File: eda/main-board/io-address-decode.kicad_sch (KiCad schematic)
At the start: 2 parts, among them U5 74HCT138

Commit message: Work on main board eda, interim
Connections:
- net IoSelect0: now also U5.15 (O0)
- net IoSelect1: now also U5.14 (O1)
- net IoSelect2: now also U5.13 (O2)
- net IoSelect3: now also U5.12 (O3)
- net IoSelect4: now also U5.11 (O4)
- net IoSelect5: now also U5.10 (O5)
- net IoSelect6: now also U5.9 (O6)
- net IoSelect7: now also U5.7 (O7)
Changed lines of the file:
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@@
     (stroke (width 0) (type default))
   )
-  (label "A8" (at 44.45 45.72 0)
+  (label "A8" (at 44.45 45.72 0) (fields_autoplaced)
     (effects (font (size 1.27 1.27)) (justify left bottom))
   )
-  (label "IoSelect5" (at 69.85 53.34 0)
+  (label "IoSelect5" (at 72.39 53.34 0) (fields_autoplaced)
     (effects (font (size 1.27 1.27)) (justify left bottom))
   )
-  (label "A6" (at 44.45 40.64 0)
+  (label "A6" (at 44.45 40.64 0) (fields_autoplaced)
     (effects (font (size 1.27 1.27)) (justify left bottom))
   )
-  (label "IoSelect1" (at 69.85 43.18 0)
+  (label "IoSelect1" (at 72.39 43.18 0) (fields_autoplaced)
     (effects (font (size 1.27 1.27)) (justify left bottom))
   )
-  (label "IoSelect0" (at 69.85 40.64 0)
+  (label "IoSelect0" (at 72.39 40.64 0) (fields_autoplaced)
     (effects (font (size 1.27 1.27)) (justify left bottom))
   )
-  (label "IoSelect2" (at 69.85 45.72 0)
+  (label "IoSelect2" (at 72.39 45.72 0) (fields_autoplaced)
     (effects (font (size 1.27 1.27)) (justify left bottom))
   )
-  (label "IoSelect4" (at 69.85 50.8 0)
+  (label "IoSelect4" (at 72.39 50.8 0) (fields_autoplaced)
     (effects (font (size 1.27 1.27)) (justify left bottom))
   )
-  (label "IoSelect7" (at 69.85 58.42 0)
+  (label "IoSelect7" (at 72.39 58.42 0) (fields_autoplaced)
     (effects (font (size 1.27 1.27)) (justify left bottom))
   )
-  (label "IoSelect6" (at 69.85 55.88 0)
+  (label "IoSelect6" (at 72.39 55.88 0) (fields_autoplaced)
     (effects (font (size 1.27 1.27)) (justify left bottom))
   )
-  (label "A7" (at 44.45 43.18 0)
+  (label "A7" (at 44.45 43.18 0) (fields_autoplaced)
     (effects (font (size 1.27 1.27)) (justify left bottom))
   )
-  (label "IoSelect3" (at 69.85 48.26 0)
+  (label "IoSelect3" (at 72.39 48.26 0) (fields_autoplaced)
     (effects (font (size 1.27 1.27)) (justify left bottom))
   )

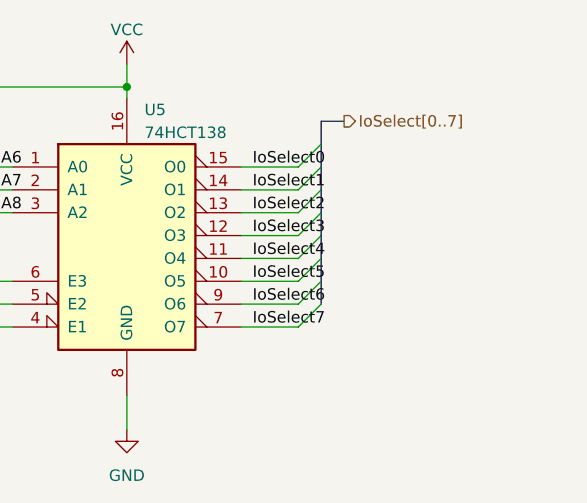
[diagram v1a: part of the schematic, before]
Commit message: EDA work for new expansion header
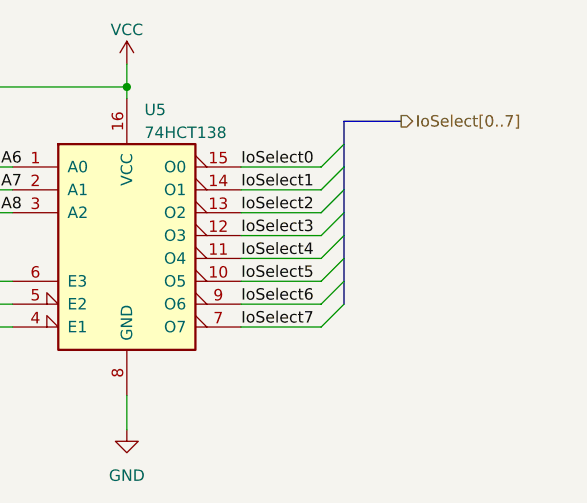
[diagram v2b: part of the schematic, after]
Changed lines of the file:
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@@
   (junction (at 41.91 58.42) (diameter 0) (color 0 0 0 0)
   )
-  (bus_entry (at 80.01 55.88) (size -2.54 2.54)
+  (bus_entry (at 82.55 55.88) (size -2.54 2.54)
     (stroke (width 0) (type default))
   )
-  (bus_entry (at 80.01 38.1) (size -2.54 2.54)
+  (bus_entry (at 82.55 38.1) (size -2.54 2.54)
     (stroke (width 0) (type default))
   )
@@
     (stroke (width 0) (type default))
   )
-  (bus_entry (at 80.01 48.26) (size -2.54 2.54)
+  (bus_entry (at 82.55 48.26) (size -2.54 2.54)
     (stroke (width 0) (type default))
   )
@@
     (stroke (width 0) (type default))
   )
-  (bus_entry (at 80.01 43.18) (size -2.54 2.54)
+  (bus_entry (at 82.55 43.18) (size -2.54 2.54)
     (stroke (width 0) (type default))
   )
-  (bus_entry (at 80.01 40.64) (size -2.54 2.54)
+  (bus_entry (at 82.55 40.64) (size -2.54 2.54)
     (stroke (width 0) (type default))
   )
@@
     (stroke (width 0) (type default))
   )
-  (bus_entry (at 80.01 50.8) (size -2.54 2.54)
+  (bus_entry (at 82.55 50.8) (size -2.54 2.54)
     (stroke (width 0) (type default))
   )
-  (bus_entry (at 80.01 45.72) (size -2.54 2.54)
+  (bus_entry (at 82.55 45.72) (size -2.54 2.54)
     (stroke (width 0) (type default))
   )
-  (bus_entry (at 80.01 53.34) (size -2.54 2.54)
+  (bus_entry (at 82.55 53.34) (size -2.54 2.54)
     (stroke (width 0) (type default))
   )
-  (bus (pts (xy 80.01 40.64) (xy 80.01 43.18))
+  (bus (pts (xy 82.55 40.64) (xy 82.55 43.18))
     (stroke (width 0) (type default))
   )
-  (wire (pts (xy 71.12 53.34) (xy 77.47 53.34))
+  (wire (pts (xy 71.12 53.34) (xy 80.01 53.34))
     (stroke (width 0) (type default))
   )
-  (bus (pts (xy 80.01 48.26) (xy 80.01 50.8))
+  (bus (pts (xy 82.55 48.26) (xy 82.55 50.8))
     (stroke (width 0) (type default))
   )
-  (wire (pts (xy 71.12 43.18) (xy 77.47 43.18))
+  (wire (pts (xy 71.12 43.18) (xy 80.01 43.18))
     (stroke (width 0) (type default))
   )
@@
     (stroke (width 0) (type default))
   )
-  (wire (pts (xy 71.12 50.8) (xy 77.47 50.8))
+  (wire (pts (xy 71.12 50.8) (xy 80.01 50.8))
     (stroke (width 0) (type default))
   )
-  (bus (pts (xy 80.01 35.56) (xy 80.01 38.1))
+  (bus (pts (xy 82.55 35.56) (xy 82.55 38.1))
     (stroke (width 0) (type default))
   )
@@
     (stroke (width 0) (type default))
   )
-  (wire (pts (xy 71.12 40.64) (xy 77.47 40.64))
+  (wire (pts (xy 71.12 40.64) (xy 80.01 40.64))
     (stroke (width 0) (type default))
   )
-  (bus (pts (xy 80.01 43.18) (xy 80.01 45.72))
+  (bus (pts (xy 82.55 43.18) (xy 82.55 45.72))
     (stroke (width 0) (type default))
   )
@@
     (stroke (width 0) (type default))
   )
-  (bus (pts (xy 82.55 35.56) (xy 80.01 35.56))
+  (bus (pts (xy 88.9 35.56) (xy 82.55 35.56))
     (stroke (width 0) (type default))
   )
@@
     (stroke (width 0) (type default))
   )
-  (bus (pts (xy 80.01 38.1) (xy 80.01 40.64))
+  (bus (pts (xy 82.55 38.1) (xy 82.55 40.64))
     (stroke (width 0) (type default))
   )
-  (bus (pts (xy 80.01 45.72) (xy 80.01 48.26))
+  (bus (pts (xy 82.55 45.72) (xy 82.55 48.26))
     (stroke (width 0) (type default))
   )
@@
     (stroke (width 0) (type default))
   )
-  (wire (pts (xy 71.12 45.72) (xy 77.47 45.72))
+  (wire (pts (xy 71.12 45.72) (xy 80.01 45.72))
     (stroke (width 0) (type default))
   )
@@
     (stroke (width 0) (type default))
   )
-  (wire (pts (xy 71.12 55.88) (xy 77.47 55.88))
+  (wire (pts (xy 71.12 55.88) (xy 80.01 55.88))
     (stroke (width 0) (type default))
   )
@@
     (stroke (width 0) (type default))
   )
-  (wire (pts (xy 71.12 48.26) (xy 77.47 48.26))
+  (wire (pts (xy 71.12 48.26) (xy 80.01 48.26))
     (stroke (width 0) (type default))
   )
-  (wire (pts (xy 71.12 58.42) (xy 77.47 58.42))
+  (wire (pts (xy 71.12 58.42) (xy 80.01 58.42))
     (stroke (width 0) (type default))
   )
@@
     (stroke (width 0) (type default))
   )
-  (bus (pts (xy 80.01 53.34) (xy 80.01 55.88))
+  (bus (pts (xy 82.55 53.34) (xy 82.55 55.88))
     (stroke (width 0) (type default))
   )
-  (bus (pts (xy 80.01 50.8) (xy 80.01 53.34))
+  (bus (pts (xy 82.55 50.8) (xy 82.55 53.34))
     (stroke (width 0) (type default))
   )
@@
     (effects (font (size 1.27 1.27)) (justify left bottom))
   )
-  (label "IoSelect5" (at 72.39 53.34 0) (fields_autoplaced)
+  (label "IoSelect5" (at 71.12 53.34 0) (fields_autoplaced)
     (effects (font (size 1.27 1.27)) (justify left bottom))
   )
@@
     (effects (font (size 1.27 1.27)) (justify left bottom))
   )
-  (label "IoSelect1" (at 72.39 43.18 0) (fields_autoplaced)
+  (label "IoSelect1" (at 71.12 43.18 0) (fields_autoplaced)
     (effects (font (size 1.27 1.27)) (justify left bottom))
   )
-  (label "IoSelect0" (at 72.39 40.64 0) (fields_autoplaced)
+  (label "IoSelect0" (at 71.12 40.64 0) (fields_autoplaced)
     (effects (font (size 1.27 1.27)) (justify left bottom))
   )
-  (label "IoSelect2" (at 72.39 45.72 0) (fields_autoplaced)
+  (label "IoSelect2" (at 71.12 45.72 0) (fields_autoplaced)
     (effects (font (size 1.27 1.27)) (justify left bottom))
   )
-  (label "IoSelect4" (at 72.39 50.8 0) (fields_autoplaced)
+  (label "IoSelect4" (at 71.12 50.8 0) (fields_autoplaced)
     (effects (font (size 1.27 1.27)) (justify left bottom))
   )
-  (label "IoSelect7" (at 72.39 58.42 0) (fields_autoplaced)
+  (label "IoSelect7" (at 71.12 58.42 0) (fields_autoplaced)
     (effects (font (size 1.27 1.27)) (justify left bottom))
   )
-  (label "IoSelect6" (at 72.39 55.88 0) (fields_autoplaced)
+  (label "IoSelect6" (at 71.12 55.88 0) (fields_autoplaced)
     (effects (font (size 1.27 1.27)) (justify left bottom))
   )
@@
     (effects (font (size 1.27 1.27)) (justify left bottom))
   )
-  (label "IoSelect3" (at 72.39 48.26 0) (fields_autoplaced)
+  (label "IoSelect3" (at 71.12 48.26 0) (fields_autoplaced)
     (effects (font (size 1.27 1.27)) (justify left bottom))
   )
@@
     (effects (font (size 1.27 1.27)) (justify right))
   )
-  (hierarchical_label "IoSelect[0..7]" (shape output) (at 82.55 35.56 0) (fields_autoplaced)
+  (hierarchical_label "IoSelect[0..7]" (shape output) (at 88.9 35.56 0) (fields_autoplaced)
     (effects (font (size 1.27 1.27)) (justify left))
   )
